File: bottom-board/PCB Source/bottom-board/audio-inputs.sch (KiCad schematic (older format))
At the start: 68 parts, among them P10 JACK_TRS_6PINS, P9 JACK_TRS_6PINS, Q1 2N7002, Q2 2N7002, Q3 J110, Q4 J110, Q5 J110, Q6 J110, Q7 2N7002, Q8 2N7002, U5 LM4562

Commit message: rev 0.0.3
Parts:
- removed FB4: Ferrite_Bead, Resistor_SMD:R_0603_1608Metric, symbol Device:Ferrite_Bead
- removed R68, R69: 10K, Resistor_SMD:R_0603_1608Metric, symbol Device:R_Small
- added C11, C13, C14, C22, C38, C53, C6: 100nF, Capacitor_SMD:C_0603_1608Metric, symbol bottom-board-rescue:C_Small
- added C72: 47uF, Capacitor_SMD:CP_Elec_5x5.4, symbol bottom-board-rescue:CP_Small
- added D3, D4: BAT54S, Package_TO_SOT_SMD:SOT-23, symbol bottom-board-rescue:BAT54S-Diode
- added R100, R70, R71, R99: 1K, Resistor_SMD:R_0603_1608Metric, symbol bottom-board-rescue:R_Small-Device
- added R101: 100R, Resistor_SMD:R_0603_1608Metric, symbol bottom-board-rescue:R_Small-Device
- C35: value 10uF -> 100nF; MPN CL10A106MQ8NNNC -> GCM188R71C104KA37D
- D5, D6, D8, D9: symbol Diode:1N4148 -> bottom-board-rescue:1N4148-Diode
- P10, P9: symbol Connector:AudioJack3_Switch -> bottom-board-rescue:AudioJack3_Switch-Connector
- Q3, Q4, Q5, Q6: value J110 -> BSR58; MPN PMBFJ110,215 -> BSR58
- R17, R18, R19, R21, R23, R24, R25, R26, R27, R28, R29, R31, R32, R33, R34, R35, R36, R37, R38, R39, R40, R44, R53, R54, R64, R66: symbol Device:R_Small -> bottom-board-rescue:R_Small-Device
- R20, R22, R65, R67: symbol Device:R_Small -> bottom-board-rescue:R_Small-Device; MPN RMCF0603JT2K70 -> CRGCQ0603F2K7
- R41, R45: value 100R 1% -> 100R; symbol Device:R_Small -> bottom-board-rescue:R_Small-Device; MPN RR0816P-101-D -> RMCF0603JT100R
- TP3, TP4, TP5, TP6, TP7: symbol Connector:TestPoint -> bottom-board-rescue:TestPoint-Connector
- U5: symbol Amplifier_Operational:TL072 -> bottom-board-rescue:TL072-Amplifier_Operational
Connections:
- net labels added: +10V, +5VA
- net labels removed: +12VA
- wire segments 193 -> 228
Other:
- moved on the sheet: Q1, Q2, Q7, Q8, R19, R20, R21, R22, R25, R26, R53, R54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

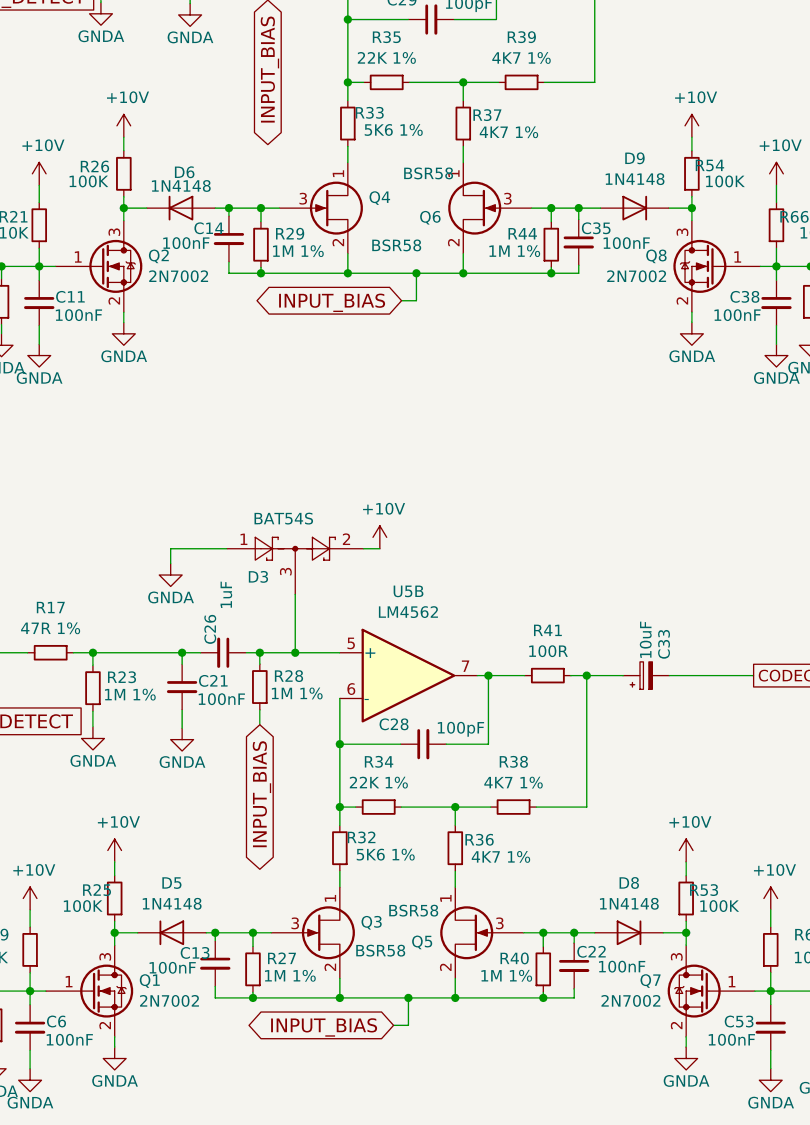
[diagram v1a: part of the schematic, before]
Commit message: change design to 4 layer PCB
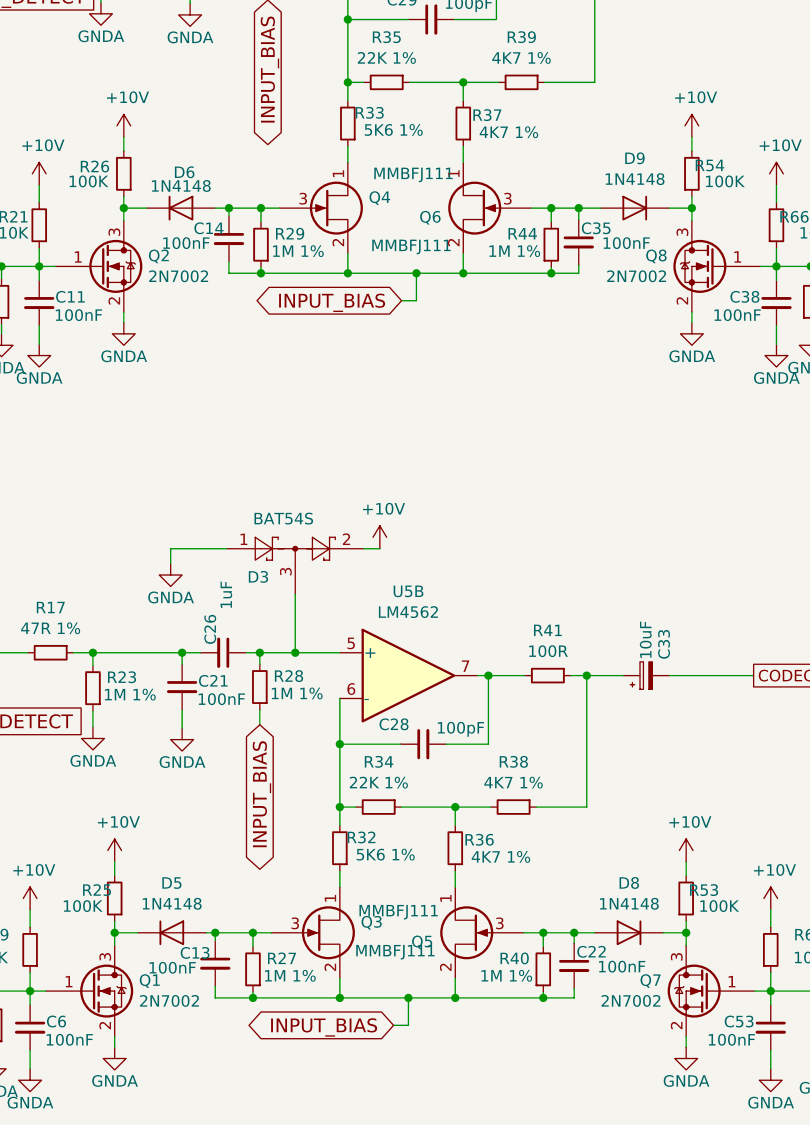
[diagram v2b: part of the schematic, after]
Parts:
- C26, C27: MPN FCA1210C105M-G2 -> TMK107B7105KA-T
- Q3, Q4, Q5, Q6: value BSR58 -> MMBFJ111; MPN BSR58 -> MMBFJ111
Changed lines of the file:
@@
 F 2 "Capacitor_SMD:C_0603_1608Metric" H 3105 1195 60  0001 C CNN
 F 3 "" H 3105 1195 60  0000 C CNN
-F 4 "FCA1210C105M-G2" H -2195 -4155 50  0001 C CNN "MPN"
+F 4 "TMK107B7105KA-T" H -2195 -4155 50  0001 C CNN "MPN"
 	1    3105 1195
 	0    1    1    0
@@
 P 3515 2420
 F 0 "Q4" H 3706 2466 50  0000 L CNN
-F 1 "BSR58" H 3715 2255 50  0000 L CNN
+F 1 "MMBFJ111" H 3715 2255 50  0000 L CNN
 F 2 "Package_TO_SOT_SMD:SOT-23" H 3715 2520 50  0001 C CNN
 F 3 "" H 3515 2420 50  0001 C CNN
-F 4 "BSR58" H 3515 2420 50  0001 C CNN "MPN"
+F 4 "MMBFJ111" H 3515 2420 50  0001 C CNN "MPN"
 	1    3515 2420
 	1    0    0    -1
@@
 P 4220 2420
 F 0 "Q6" H 4415 2380 50  0000 L CNN
-F 1 "BSR58" H 4360 2570 50  0000 L CNN
+F 1 "MMBFJ111" H 4360 2570 50  0000 L CNN
 F 2 "Package_TO_SOT_SMD:SOT-23" H 4420 2520 50  0001 C CNN
 F 3 "" H 4220 2420 50  0001 C CNN
-F 4 "BSR58" H 4220 2420 50  0001 C CNN "MPN"
+F 4 "MMBFJ111" H 4220 2420 50  0001 C CNN "MPN"
 	1    4220 2420
 	-1   0    0    -1
@@
 F 2 "Capacitor_SMD:C_0603_1608Metric" H 3070 4365 60  0001 C CNN
 F 3 "" H 3070 4365 60  0000 C CNN
-F 4 "FCA1210C105M-G2" H -2230 -985 50  0001 C CNN "MPN"
+F 4 "TMK107B7105KA-T" H -2230 -985 50  0001 C CNN "MPN"
 	1    3070 4365
 	0    1    1    0
@@
 P 3480 5590
 F 0 "Q3" H 3671 5636 50  0000 L CNN
-F 1 "BSR58" H 3645 5510 50  0000 L CNN
+F 1 "MMBFJ111" H 3645 5510 50  0000 L CNN
 F 2 "Package_TO_SOT_SMD:SOT-23" H 3680 5690 50  0001 C CNN
 F 3 "" H 3480 5590 50  0001 C CNN
-F 4 "BSR58" H 3480 5590 50  0001 C CNN "MPN"
+F 4 "MMBFJ111" H 3480 5590 50  0001 C CNN "MPN"
 	1    3480 5590
 	1    0    0    -1
@@
 P 4185 5590
 F 0 "Q5" H 4380 5550 50  0000 L CNN
-F 1 "BSR58" H 4355 5685 50  0000 L CNN
+F 1 "MMBFJ111" H 4355 5685 50  0000 L CNN
 F 2 "Package_TO_SOT_SMD:SOT-23" H 4385 5690 50  0001 C CNN
 F 3 "" H 4185 5590 50  0001 C CNN
-F 4 "BSR58" H 4185 5590 50  0001 C CNN "MPN"
+F 4 "MMBFJ111" H 4185 5590 50  0001 C CNN "MPN"
 	1    4185 5590
 	-1   0    0    -1

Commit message: minor cleanup
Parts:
- C21, C23: value 100nF -> 100pF; MPN GCM188R71C104KA37D -> C0603C101J3GACTU
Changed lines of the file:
@@
 AR Path="/54F72C8D/5F11DD8E" Ref="C23"  Part="1"
 F 0 "C23" H 2995 1370 50  0000 L CNN
-F 1 "100nF" H 2990 1290 50  0000 L CNN
+F 1 "100pF" H 2990 1290 50  0000 L CNN
 F 2 "Capacitor_SMD:C_0603_1608Metric" H 2925 1345 60  0001 C CNN
 F 3 "" H 2925 1345 60  0000 C CNN
-F 4 "GCM188R71C104KA37D" H -2375 -4005 50  0001 C CNN "MPN"
+F 4 "C0603C101J3GACTU" H -2375 -4005 50  0001 C CNN "MPN"
 	1    2925 1345
 	1    0    0    -1
@@
 AR Path="/54F72C8D/5F23421C" Ref="C21"  Part="1"
 F 0 "C21" H 2960 4540 50  0000 L CNN
-F 1 "100nF" H 2955 4460 50  0000 L CNN
+F 1 "100pF" H 2955 4460 50  0000 L CNN
 F 2 "Capacitor_SMD:C_0603_1608Metric" H 2890 4515 60  0001 C CNN
 F 3 "" H 2890 4515 60  0000 C CNN
-F 4 "GCM188R71C104KA37D" H -2410 -835 50  0001 C CNN "MPN"
+F 4 "C0603C101J3GACTU" H -2410 -835 50  0001 C CNN "MPN"
 	1    2890 4515
 	1    0    0    -1

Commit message: cleanup BOM lines
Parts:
- C37: MPN CL10A106MQ8NNNC -> EMK107BBJ106MA-T
- Q3, Q4, Q5, Q6: value MMBFJ111 -> MMBFJ110; MPN MMBFJ111 -> MMBFJ110
- R100, R70, R71, R99: MPN RC0603JR-071KL -> ERJ-PB3D1001V
- R101: value 100R -> 1K; MPN RMCF0603JT100R -> ERJ-PB3D1001V
- R14, R15: MPN CR0603-JW-104ELF -> RMCF0603JT100K
- R32, R33: MPN CRGCQ0603F5K6 -> ERA-3AED562V
- R34, R35: MPN RC0603FR-0722KL -> RT0603DRD0722KL
- R36, R37, R38, R39: MPN RC0603FR-074K7L -> RT0603DRE074K7L
- R41, R45: MPN RMCF0603JT100R -> RT0603DRD07100RL
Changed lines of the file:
@@
 encoding utf-8
 Sheet 5 11
-Title "MOD Uno - Main Board"
-Date "2019-08-16"
-Rev "0.1"
+Title "MOD Dwarf - Main Board"
+Date "2021-04-07"
+Rev "1.2"
 Comp "MOD Devices GmbH"
-Comment1 "Uno Audio processing board"
-Comment2 "https://github.com/moddevices/hw-mod-uno"
+Comment1 "Dwarf Audio processing board"
+Comment2 "https://github.com/moddevices/hw-mod-dwarf"
 Comment3 "Inp Power: 12V 500mA"
 Comment4 "USB outp Power: 500mA"
@@
 F 2 "Resistor_SMD:R_0603_1608Metric" H 4525 1295 50  0001 C CNN
 F 3 "" H 4525 1295 50  0001 C CNN
-F 4 "RMCF0603JT100R" V 4525 1295 50  0001 C CNN "MPN"
+F 4 "RT0603DRD07100RL" V 4525 1295 50  0001 C CNN "MPN"
 	1    4525 1295
 	0    1    1    0
@@
 F 2 "Resistor_SMD:R_0603_1608Metric" H 4375 1870 50  0001 C CNN
 F 3 "~" H 4375 1870 50  0001 C CNN
-F 4 "RC0603FR-074K7L" V 4375 1870 50  0001 C CNN "MPN"
+F 4 "RT0603DRE074K7L" V 4375 1870 50  0001 C CNN "MPN"
 	1    4375 1870
 	0    1    1    0
@@
 F 2 "Resistor_SMD:R_0603_1608Metric" H 3785 1870 50  0001 C CNN
 F 3 "" H 3785 1870 50  0001 C CNN
-F 4 "RC0603FR-0722KL" V 3785 1870 50  0001 C CNN "MPN"
+F 4 "RT0603DRD0722KL" V 3785 1870 50  0001 C CNN "MPN"
 	1    3785 1870
 	0    1    1    0
@@
 U 1 1 5F14FEBE
 P 3615 2050
-F 0 "R33" H 3520 2005 50  0000 C CNN
+F 0 "R33" H 3495 1995 50  0000 C CNN
 F 1 "5K6 1%" H 3415 2080 50  0000 C CNN
 F 2 "Resistor_SMD:R_0603_1608Metric" H 3615 2050 50  0001 C CNN
 F 3 "~" H 3615 2050 50  0001 C CNN
-F 4 "CRGCQ0603F5K6" V 3615 2050 50  0001 C CNN "MPN"
+F 4 "ERA-3AED562V" V 3615 2050 50  0001 C CNN "MPN"
 	1    3615 2050
 	-1   0    0    1
@@
 F 2 "Resistor_SMD:R_0603_1608Metric" H 4120 2050 50  0001 C CNN
 F 3 "~" H 4120 2050 50  0001 C CNN
-F 4 "RC0603FR-074K7L" V 4120 2050 50  0001 C CNN "MPN"
+F 4 "RT0603DRE074K7L" V 4120 2050 50  0001 C CNN "MPN"
 	1    4120 2050
 	-1   0    0    1
@@
 P 3515 2420
 F 0 "Q4" H 3706 2466 50  0000 L CNN
-F 1 "MMBFJ111" H 3715 2255 50  0000 L CNN
+F 1 "MMBFJ110" H 3715 2255 50  0000 L CNN
 F 2 "Package_TO_SOT_SMD:SOT-23" H 3715 2520 50  0001 C CNN
 F 3 "" H 3515 2420 50  0001 C CNN
-F 4 "MMBFJ111" H 3515 2420 50  0001 C CNN "MPN"
+F 4 "MMBFJ110" H 3515 2420 50  0001 C CNN "MPN"
 	1    3515 2420
 	1    0    0    -1
@@
 P 4220 2420
 F 0 "Q6" H 4415 2380 50  0000 L CNN
-F 1 "MMBFJ111" H 4360 2570 50  0000 L CNN
+F 1 "MMBFJ110" H 4360 2570 50  0000 L CNN
 F 2 "Package_TO_SOT_SMD:SOT-23" H 4420 2520 50  0001 C CNN
 F 3 "" H 4220 2420 50  0001 C CNN
-F 4 "MMBFJ111" H 4220 2420 50  0001 C CNN "MPN"
+F 4 "MMBFJ110" H 4220 2420 50  0001 C CNN "MPN"
 	1    4220 2420
 	-1   0    0    -1
@@
 F 1 "100K" H 2880 2305 50  0000 R CNN
 F 2 "Resistor_SMD:R_0603_1608Metric" H 2635 2270 50  0001 C CNN
-F 3 "~" H 2635 2270 50  0001 C CNN
+F 3 "" H 2635 2270 50  0001 C CNN
 F 4 "RMCF0603JT100K" V 2635 2270 50  0001 C CNN "MPN"
 	1    2635 2270
@@
 U 1 1 5F1DFDB9
 P 5120 2270
-F 0 "R54" H 5265 2235 50  0000 R CNN
+F 0 "R54" H 5320 2230 50  0000 R CNN
 F 1 "100K" H 5350 2305 50  0000 R CNN
 F 2 "Resistor_SMD:R_0603_1608Metric" H 5120 2270 50  0001 C CNN
-F 3 "~" H 5120 2270 50  0001 C CNN
+F 3 "" H 5120 2270 50  0001 C CNN
 F 4 "RMCF0603JT100K" V 5120 2270 50  0001 C CNN "MPN"
 	1    5120 2270
@@
 U 1 1 5F1DFDD1
 P 5490 2495
-F 0 "R66" H 5635 2460 50  0000 R CNN
+F 0 "R66" H 5680 2455 50  0000 R CNN
 F 1 "10K" H 5720 2530 50  0000 R CNN
 F 2 "Resistor_SMD:R_0603_1608Metric" H 5490 2495 50  0001 C CNN
@@
 F 2 "Resistor_SMD:R_0603_1608Metric" H 4490 4465 50  0001 C CNN
 F 3 "" H 4490 4465 50  0001 C CNN
-F 4 "RMCF0603JT100R" V 4490 4465 50  0001 C CNN "MPN"
+F 4 "RT0603DRD07100RL" V 4490 4465 50  0001 C CNN "MPN"
 	1    4490 4465
 	0    1    1    0
@@
 F 2 "Resistor_SMD:R_0603_1608Metric" H 4340 5040 50  0001 C CNN
 F 3 "~" H 4340 5040 50  0001 C CNN
-F 4 "RC0603FR-074K7L" V 4340 5040 50  0001 C CNN "MPN"
+F 4 "RT0603DRE074K7L" V 4340 5040 50  0001 C CNN "MPN"
 	1    4340 5040
 	0    1    1    0
@@
 F 2 "Resistor_SMD:R_0603_1608Metric" H 3750 5040 50  0001 C CNN
 F 3 "" H 3750 5040 50  0001 C CNN
-F 4 "RC0603FR-0722KL" V 3750 5040 50  0001 C CNN "MPN"
+F 4 "RT0603DRD0722KL" V 3750 5040 50  0001 C CNN "MPN"
 	1    3750 5040
 	0    1    1    0
@@
 U 1 1 5F23427C
 P 3580 5220
-F 0 "R32" H 3485 5175 50  0000 C CNN
+F 0 "R32" H 3470 5175 50  0000 C CNN
 F 1 "5K6 1%" H 3380 5250 50  0000 C CNN
 F 2 "Resistor_SMD:R_0603_1608Metric" H 3580 5220 50  0001 C CNN
 F 3 "~" H 3580 5220 50  0001 C CNN
-F 4 "CRGCQ0603F5K6" V 3580 5220 50  0001 C CNN "MPN"
+F 4 "ERA-3AED562V" V 3580 5220 50  0001 C CNN "MPN"
 	1    3580 5220
 	-1   0    0    1
@@
 F 2 "Resistor_SMD:R_0603_1608Metric" H 4085 5220 50  0001 C CNN
 F 3 "~" H 4085 5220 50  0001 C CNN
-F 4 "RC0603FR-074K7L" V 4085 5220 50  0001 C CNN "MPN"
+F 4 "RT0603DRE074K7L" V 4085 5220 50  0001 C CNN "MPN"
 	1    4085 5220
 	-1   0    0    1
@@
 P 3480 5590
 F 0 "Q3" H 3671 5636 50  0000 L CNN
-F 1 "MMBFJ111" H 3645 5510 50  0000 L CNN
+F 1 "MMBFJ110" H 3645 5510 50  0000 L CNN
 F 2 "Package_TO_SOT_SMD:SOT-23" H 3680 5690 50  0001 C CNN
 F 3 "" H 3480 5590 50  0001 C CNN
-F 4 "MMBFJ111" H 3480 5590 50  0001 C CNN "MPN"
+F 4 "MMBFJ110" H 3480 5590 50  0001 C CNN "MPN"
 	1    3480 5590
 	1    0    0    -1
@@
 P 4185 5590
 F 0 "Q5" H 4380 5550 50  0000 L CNN
-F 1 "MMBFJ111" H 4355 5685 50  0000 L CNN
+F 1 "MMBFJ110" H 4355 5685 50  0000 L CNN
 F 2 "Package_TO_SOT_SMD:SOT-23" H 4385 5690 50  0001 C CNN
 F 3 "" H 4185 5590 50  0001 C CNN
-F 4 "MMBFJ111" H 4185 5590 50  0001 C CNN "MPN"
+F 4 "MMBFJ110" H 4185 5590 50  0001 C CNN "MPN"
 	1    4185 5590
 	-1   0    0    -1
@@
 U 1 1 5F2342BF
 P 2595 5440
-F 0 "R25" H 2740 5405 50  0000 R CNN
+F 0 "R25" H 2815 5375 50  0000 R CNN
 F 1 "100K" H 2825 5475 50  0000 R CNN
 F 2 "Resistor_SMD:R_0603_1608Metric" H 2595 5440 50  0001 C CNN
-F 3 "~" H 2595 5440 50  0001 C CNN
+F 3 "" H 2595 5440 50  0001 C CNN
 F 4 "RMCF0603JT100K" V 2595 5440 50  0001 C CNN "MPN"
 	1    2595 5440
@@
 F 2 "Capacitor_SMD:C_0603_1608Metric" H 9430 5295 60  0001 C CNN
 F 3 "" H 9430 5295 60  0000 C CNN
-F 4 "CL10A106MQ8NNNC" H 4980 3595 50  0001 C CNN "MPN"
+F 4 "EMK107BBJ106MA-T" H 4980 3595 50  0001 C CNN "MPN"
 	1    9430 5295
 	-1   0    0    1
@@
 F 2 "Resistor_SMD:R_0603_1608Metric" H 1640 4865 60  0001 C CNN
 F 3 "" H 1640 4865 60  0000 C CNN
-F 4 "CR0603-JW-104ELF" H 1640 4865 50  0001 C CNN "MPN"
+F 4 "RMCF0603JT100K" H 1640 4865 50  0001 C CNN "MPN"
 	1    1640 4865
 	1    0    0    1
@@
 F 2 "Resistor_SMD:R_0603_1608Metric" H 1620 1695 60  0001 C CNN
 F 3 "" H 1620 1695 60  0000 C CNN
-F 4 "CR0603-JW-104ELF" H 1620 1695 50  0001 C CNN "MPN"
+F 4 "RMCF0603JT100K" H 1620 1695 50  0001 C CNN "MPN"
 	1    1620 1695
 	1    0    0    1
@@
 P 7995 4990
 F 0 "R101" H 8250 4950 50  0000 R CNN
-F 1 "100R" H 8225 5025 50  0000 R CNN
+F 1 "1K" H 8225 5025 50  0000 R CNN
 F 2 "Resistor_SMD:R_0603_1608Metric" H 7995 4990 50  0001 C CNN
-F 3 "" H 7995 4990 50  0001 C CNN
-F 4 "RMCF0603JT100R" V 7995 4990 50  0001 C CNN "MPN"
+F 3 "~" H 7995 4990 50  0001 C CNN
+F 4 "ERJ-PB3D1001V" V 7995 4990 50  0001 C CNN "MPN"
 	1    7995 4990
 	1    0    0    1
@@
 F 2 "Resistor_SMD:R_0603_1608Metric" H 1875 2675 50  0001 C CNN
 F 3 "~" H 1875 2675 50  0001 C CNN
-F 4 "RC0603JR-071KL" H 1875 2675 50  0001 C CNN "MPN"
+F 4 "ERJ-PB3D1001V" H 1875 2675 50  0001 C CNN "MPN"
 	1    1875 2675
 	0    -1   -1   0
@@
 F 2 "Resistor_SMD:R_0603_1608Metric" H 5830 2675 50  0001 C CNN
 F 3 "~" H 5830 2675 50  0001 C CNN
-F 4 "RC0603JR-071KL" H 5830 2675 50  0001 C CNN "MPN"
+F 4 "ERJ-PB3D1001V" H 5830 2675 50  0001 C CNN "MPN"
 	1    5830 2675
 	0    1    -1   0
@@
 U 1 1 5F8BE9B7
 P 1870 5845
-F 0 "R70" H 2050 5810 50  0000 R CNN
+F 0 "R70" H 2095 5815 50  0000 R CNN
 F 1 "1K" H 2055 5880 50  0000 R CNN
 F 2 "Resistor_SMD:R_0603_1608Metric" H 1870 5845 50  0001 C CNN
 F 3 "~" H 1870 5845 50  0001 C CNN
-F 4 "RC0603JR-071KL" H 1870 5845 50  0001 C CNN "MPN"
+F 4 "ERJ-PB3D1001V" H 1870 5845 50  0001 C CNN "MPN"
 	1    1870 5845
 	0    -1   -1   0
@@
 F 2 "Resistor_SMD:R_0603_1608Metric" H 5890 5845 50  0001 C CNN
 F 3 "~" H 5890 5845 50  0001 C CNN
-F 4 "RC0603JR-071KL" H 5890 5845 50  0001 C CNN "MPN"
+F 4 "ERJ-PB3D1001V" H 5890 5845 50  0001 C CNN "MPN"
 	1    5890 5845
 	0    1    -1   0
@@
 U 1 1 5F23431A
 P 5095 5440
-F 0 "R53" H 5240 5405 50  0000 R CNN
+F 0 "R53" H 5315 5390 50  0000 R CNN
 F 1 "100K" H 5325 5475 50  0000 R CNN
 F 2 "Resistor_SMD:R_0603_1608Metric" H 5095 5440 50  0001 C CNN
-F 3 "~" H 5095 5440 50  0001 C CNN
+F 3 "" H 5095 5440 50  0001 C CNN
 F 4 "RMCF0603JT100K" V 5095 5440 50  0001 C CNN "MPN"
 	1    5095 5440

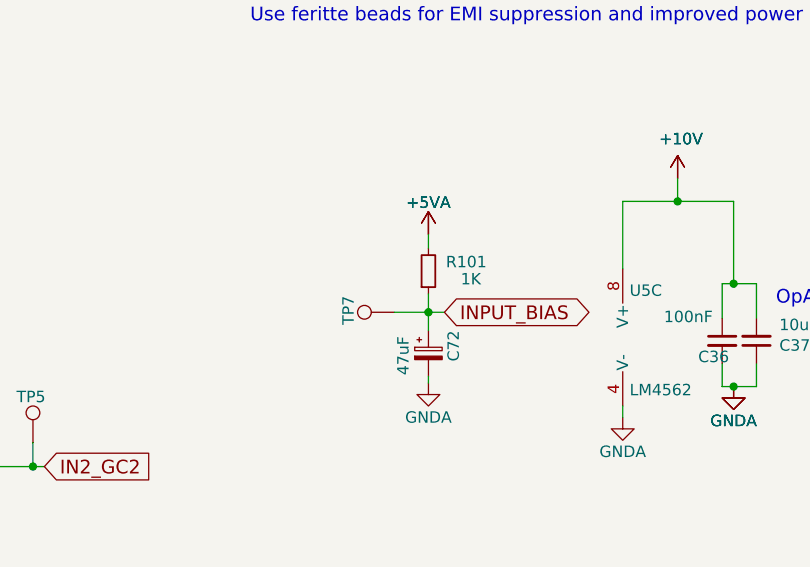
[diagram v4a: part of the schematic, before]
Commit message: change input bias from 5 to 6 volts
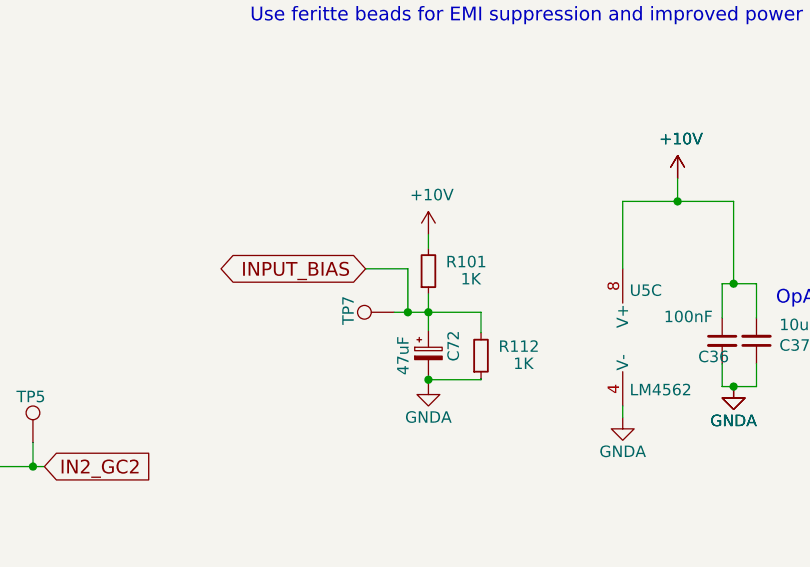
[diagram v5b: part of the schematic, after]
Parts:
- added R112: 1K, Resistor_SMD:R_0603_1608Metric, symbol bottom-board-rescue:R_Small-Device
- R101: MPN ERJ-PB3D1001V -> ERJ-PB3D1501V
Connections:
- net +5VA is gone; now on net +10V: R101.2
- net GNDA: now also R112.1
- net INPUT_BIAS: now also R112.2
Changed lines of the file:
@@
 	1    0    0    -1
 $EndComp
-Text GLabel 8065 5170 2    60   BiDi ~ 0
+Text GLabel 7720 4980 0    60   BiDi ~ 0
 INPUT_BIAS
 $Comp
@@
 $EndComp
 Wire Wire Line
-	8065 5170 7995 5170
-Wire Wire Line
 	7995 5250 7995 5170
 Wire Wire Line
-	7995 5450 7995 5480
+	7995 5450 7995 5465
 Wire Wire Line
 	9330 4685 9330 5045
@@
 	3385 4365 3230 4365
 Wire Wire Line
-	7845 5170 7995 5170
+	7845 5170 7905 5170
 Connection ~ 7995 5170
 $Comp
@@
 F 2 "Resistor_SMD:R_0603_1608Metric" H 7995 4990 50  0001 C CNN
 F 3 "~" H 7995 4990 50  0001 C CNN
-F 4 "ERJ-PB3D1001V" V 7995 4990 50  0001 C CNN "MPN"
+F 4 "ERJ-PB3D1501V" V 7995 4990 50  0001 C CNN "MPN"
 	1    7995 4990
 	1    0    0    1
-$EndComp
-$Comp
-L bottom-board-rescue:+5VA-power #PWR?
-U 1 1 5F794305
-P 7995 4830
-AR Path="/54F7244B/5F794305" Ref="#PWR?"  Part="1"
-AR Path="/54F72C8D/5F794305" Ref="#PWR0249"  Part="1"
-F 0 "#PWR0249" H 7995 4680 50  0001 C CNN
-F 1 "+5VA" H 7995 4970 50  0000 C CNN
-F 2 "" H 7995 4830 60  0000 C CNN
-F 3 "" H 7995 4830 60  0000 C CNN
-	1    7995 4830
-	1    0    0    -1
 $EndComp
 Wire Wire Line
@@
 $EndComp
 $Comp
-L bottom-board-rescue:+5VA-power #PWR?
-U 1 1 5FB7BD96
-P 7995 4830
-AR Path="/54F7244B/5FB7BD96" Ref="#PWR?"  Part="1"
-AR Path="/54F72C8D/5FB7BD96" Ref="#PWR0259"  Part="1"
-F 0 "#PWR0259" H 7995 4680 50  0001 C CNN
-F 1 "+5VA" H 7995 4970 50  0000 C CNN
-F 2 "" H 7995 4830 60  0000 C CNN
-F 3 "" H 7995 4830 60  0000 C CNN
-	1    7995 4830
-	1    0    0    -1
-$EndComp
-$Comp
 L bottom-board-rescue:+10V-power #PWR?
 U 1 1 5FB7BDA0
@@
 Wire Wire Line
 	5990 5845 6265 5845
+$Comp
+L bottom-board-rescue:R_Small-Device R112
+U 1 1 613394A3
+P 8225 5360
+F 0 "R112" H 8480 5320 50  0000 R CNN
+F 1 "1K" H 8455 5395 50  0000 R CNN
+F 2 "Resistor_SMD:R_0603_1608Metric" H 8225 5360 50  0001 C CNN
+F 3 "~" H 8225 5360 50  0001 C CNN
+F 4 "ERJ-PB3D1001V" V 8225 5360 50  0001 C CNN "MPN"
+	1    8225 5360
+	1    0    0    1
+$EndComp
+$Comp
+L bottom-board-rescue:+10V-power #PWR?
+U 1 1 61342566
+P 7995 4830
+AR Path="/54F7244B/61342566" Ref="#PWR?"  Part="1"
+AR Path="/54F72C8D/61342566" Ref="#PWR0249"  Part="1"
+F 0 "#PWR0249" H 7995 4680 50  0001 C CNN
+F 1 "+10V" H 8010 5003 50  0000 C CNN
+F 2 "" H 7995 4830 50  0001 C CNN
+F 3 "" H 7995 4830 50  0001 C CNN
+	1    7995 4830
+	1    0    0    -1
+$EndComp
+Wire Wire Line
+	8225 5260 8225 5170
+Wire Wire Line
+	7995 5170 8225 5170
+Wire Wire Line
+	8225 5460 8225 5465
+Wire Wire Line
+	8225 5465 7995 5465
+Connection ~ 7995 5465
+Wire Wire Line
+	7995 5465 7995 5480
+Wire Wire Line
+	7720 4980 7905 4980
+Wire Wire Line
+	7905 4980 7905 5170
+Connection ~ 7905 5170
+Wire Wire Line
+	7905 5170 7995 5170
 $EndSCHEMATC
